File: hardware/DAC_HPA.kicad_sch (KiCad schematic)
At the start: 0 parts

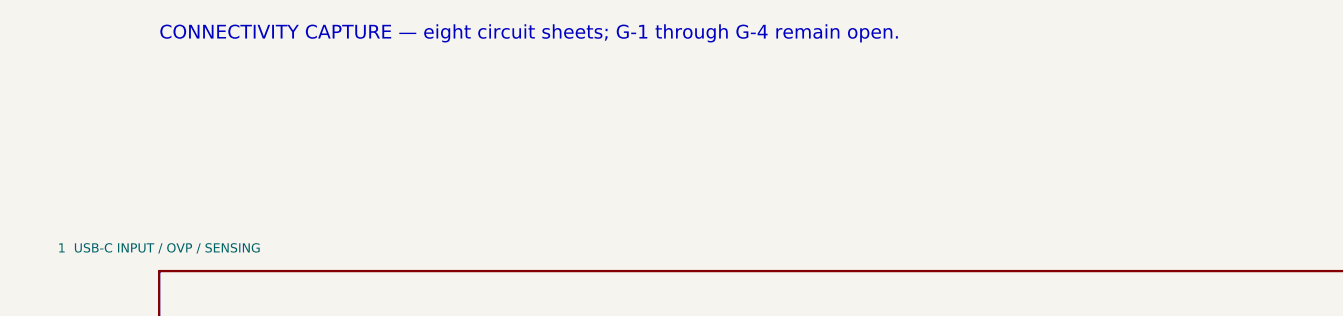
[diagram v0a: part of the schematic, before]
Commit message: Recapture DAC-HPA schematic for design set v1.1
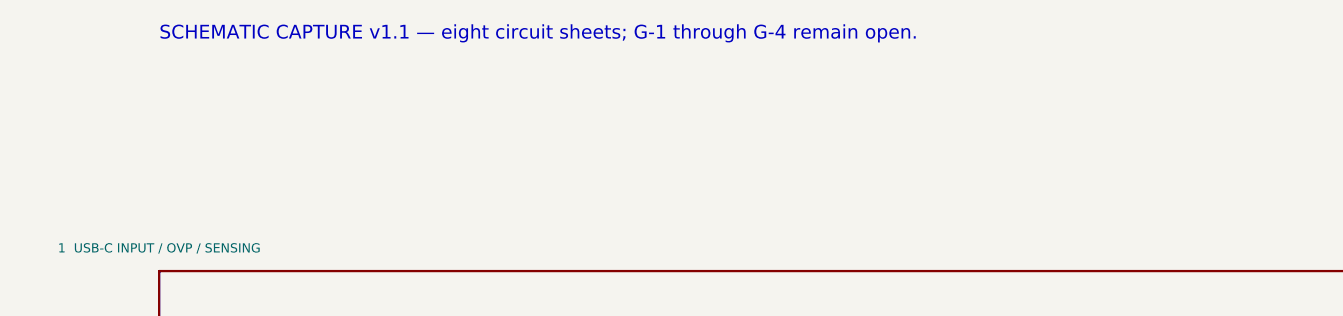
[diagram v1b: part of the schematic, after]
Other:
- note added: "SCHEMATIC CAPTURE v1.1 — eight circuit sheets; G-1 through G-4 remain open."
- note removed: "CONNECTIVITY CAPTURE — eight circuit sheets; G-1 through G-4 remain open."
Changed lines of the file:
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@@
 (generator_version "10.0")
 (paper "A3")
-(title_block (title "USB DAC + Balanced Headphone Amplifier") (date "2026-09-26") (rev "Schematic capture v1.0") (comment 1 "Design Spec v1.0 / Notes v0.9 / Parts List v0.8") (comment 2 "Connector pin maps and footprint/polarity gates remain open"))
-(text "CONNECTIVITY CAPTURE — eight circuit sheets; G-1 through G-4 remain open." (exclude_from_sim no) (at 25.4 25.4 0) (effects (font (size 1.524 1.524)) (justify left bottom)))
+(title_block (title "USB DAC + Balanced Headphone Amplifier") (date "2026-09-27") (rev "v1.1") (comment 1 "Design Spec v1.1 / Notes v1.0 / Parts List v0.9") (comment 2 "J701/J702 maps from maker drawings; G-1 to G-4 remain open"))
+(text "SCHEMATIC CAPTURE v1.1 — eight circuit sheets; G-1 through G-4 remain open." (exclude_from_sim no) (at 25.4 25.4 0) (effects (font (size 1.524 1.524)) (justify left bottom)))
 (sheet (at 25.4 50.8) (size 152.4 31.75) (stroke (width 0.254) (type default)) (fill (color 0 0 0 0)) (property "Sheetname" "1  USB-C INPUT / OVP / SENSING" (at 25.4 48.26 0) (effects (font (size 1.016 1.016)))) (property "Sheetfile" "01_usb_input.kicad_sch" (at 25.4 85.09 0) (effects (font (size 1.016 1.016)))) (instances (project "DAC_HPA" (path "/0c6c0976-e401-5c8a-8977-bc60da031e5e" (page "2")))))
 (sheet (at 215.9 50.8) (size 152.4 31.75) (stroke (width 0.254) (type default)) (fill (color 0 0 0 0)) (property "Sheetname" "2  USB AUDIO BRIDGE / CPLD / CLOCKS" (at 215.9 48.26 0) (effects (font (size 1.016 1.016)))) (property "Sheetfile" "02_usb_bridge.kicad_sch" (at 215.9 85.09 0) (effects (font (size 1.016 1.016)))) (instances (project "DAC_HPA" (path "/0c6c0976-e401-5c8a-8977-bc60da031e5e" (page "3")))))

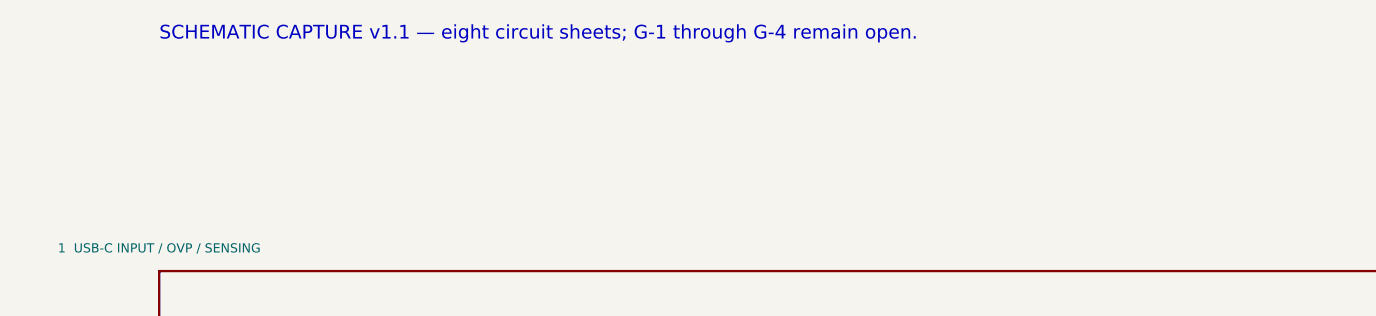
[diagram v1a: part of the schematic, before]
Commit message: Capture functional ECO and manual 120x100 review board
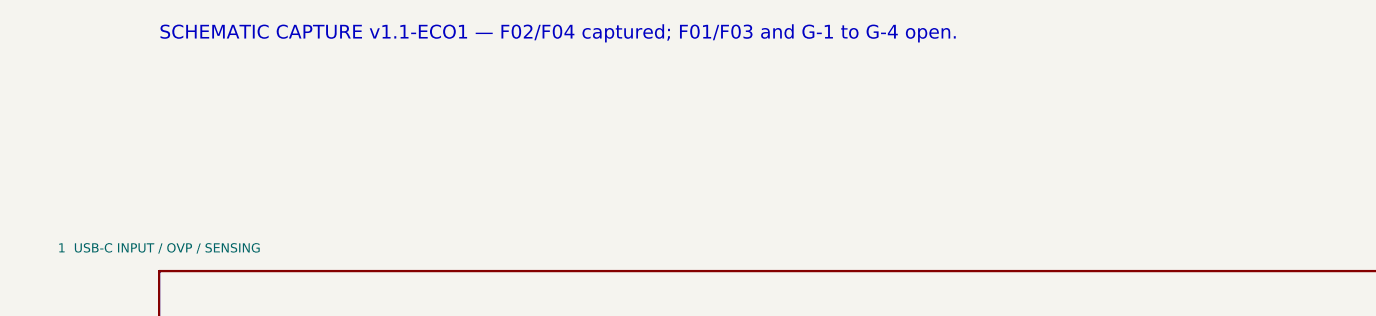
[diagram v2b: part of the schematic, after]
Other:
- note added: "SCHEMATIC CAPTURE v1.1-ECO1 — F02/F04 captured; F01/F03 and G-1 to G-4 open."
- note removed: "SCHEMATIC CAPTURE v1.1 — eight circuit sheets; G-1 through G-4 remain open."
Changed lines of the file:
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@@
 (generator_version "10.0")
 (paper "A3")
-(title_block (title "USB DAC + Balanced Headphone Amplifier") (date "2026-09-27") (rev "v1.1") (comment 1 "Design Spec v1.1 / Notes v1.0 / Parts List v0.9") (comment 2 "J701/J702 maps from maker drawings; G-1 to G-4 remain open"))
-(text "SCHEMATIC CAPTURE v1.1 — eight circuit sheets; G-1 through G-4 remain open." (exclude_from_sim no) (at 25.4 25.4 0) (effects (font (size 1.524 1.524)) (justify left bottom)))
+(title_block (title "USB DAC + Balanced Headphone Amplifier") (date "2026-09-28") (rev "v1.1-ECO1") (comment 1 "Spec v1.1 / Notes v1.0 / Parts List v0.9 + ECO F02/F04") (comment 2 "REVIEW ONLY: capture F01, attach F03 and G-1 to G-4 open"))
+(text "SCHEMATIC CAPTURE v1.1-ECO1 — F02/F04 captured; F01/F03 and G-1 to G-4 open." (exclude_from_sim no) (at 25.4 25.4 0) (effects (font (size 1.524 1.524)) (justify left bottom)))
 (sheet (at 25.4 50.8) (size 152.4 31.75) (stroke (width 0.254) (type default)) (fill (color 0 0 0 0)) (property "Sheetname" "1  USB-C INPUT / OVP / SENSING" (at 25.4 48.26 0) (effects (font (size 1.016 1.016)))) (property "Sheetfile" "01_usb_input.kicad_sch" (at 25.4 85.09 0) (effects (font (size 1.016 1.016)))) (instances (project "DAC_HPA" (path "/0c6c0976-e401-5c8a-8977-bc60da031e5e" (page "2")))))
 (sheet (at 215.9 50.8) (size 152.4 31.75) (stroke (width 0.254) (type default)) (fill (color 0 0 0 0)) (property "Sheetname" "2  USB AUDIO BRIDGE / CPLD / CLOCKS" (at 215.9 48.26 0) (effects (font (size 1.016 1.016)))) (property "Sheetfile" "02_usb_bridge.kicad_sch" (at 215.9 85.09 0) (effects (font (size 1.016 1.016)))) (instances (project "DAC_HPA" (path "/0c6c0976-e401-5c8a-8977-bc60da031e5e" (page "3")))))
